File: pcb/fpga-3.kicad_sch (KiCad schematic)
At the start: 1 part

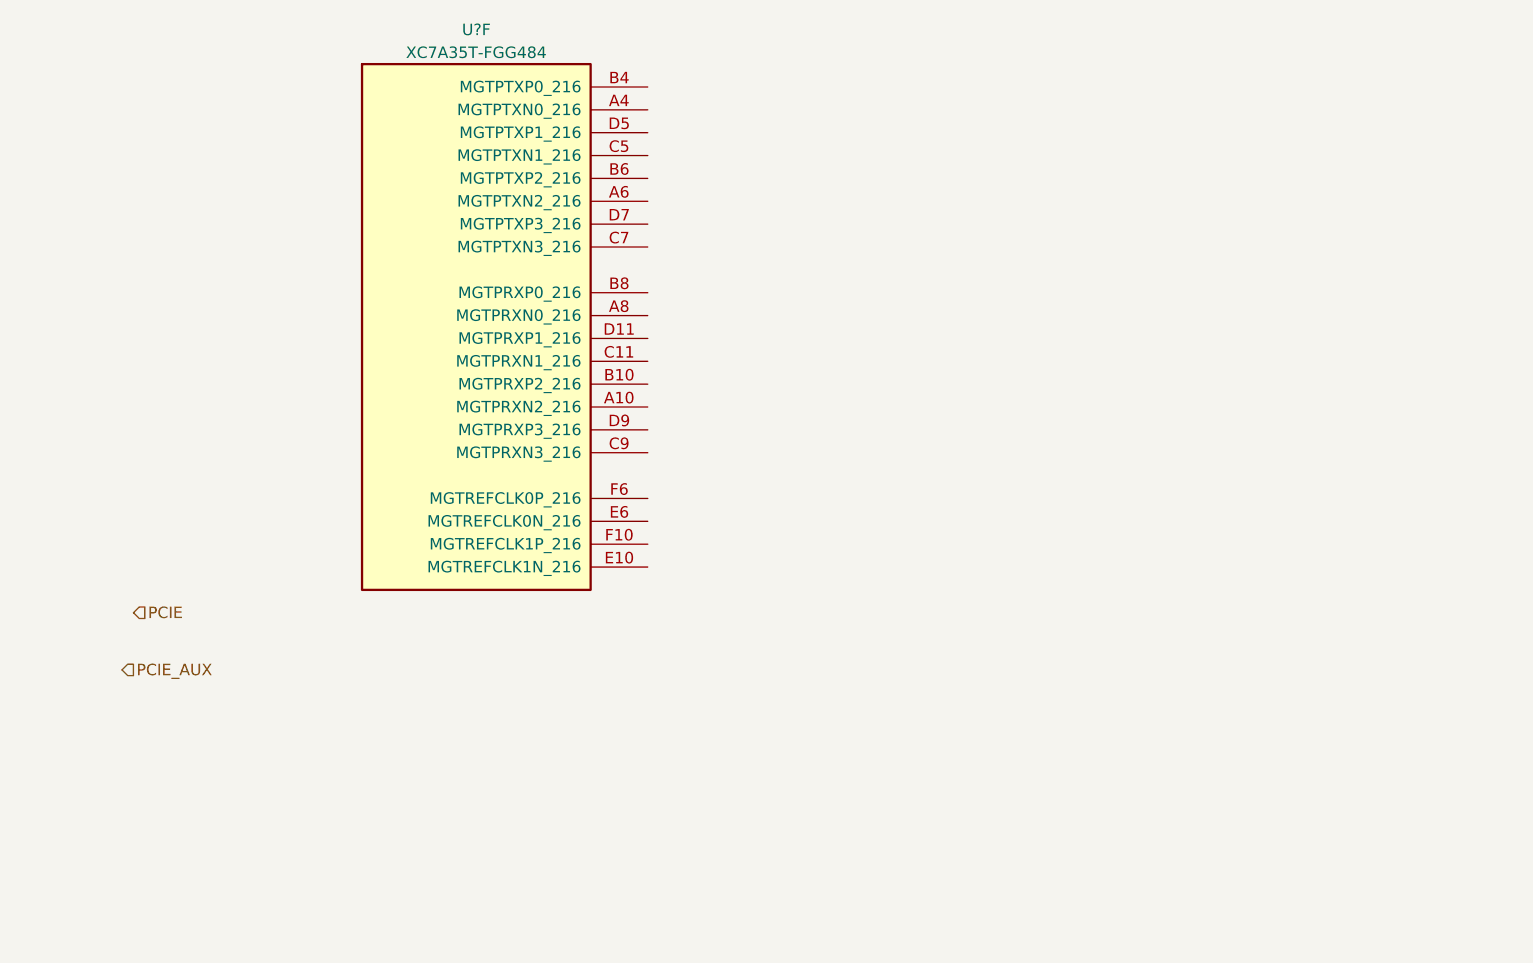
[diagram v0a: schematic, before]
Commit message: current sense, fpga power sequencing
plus restructuring files
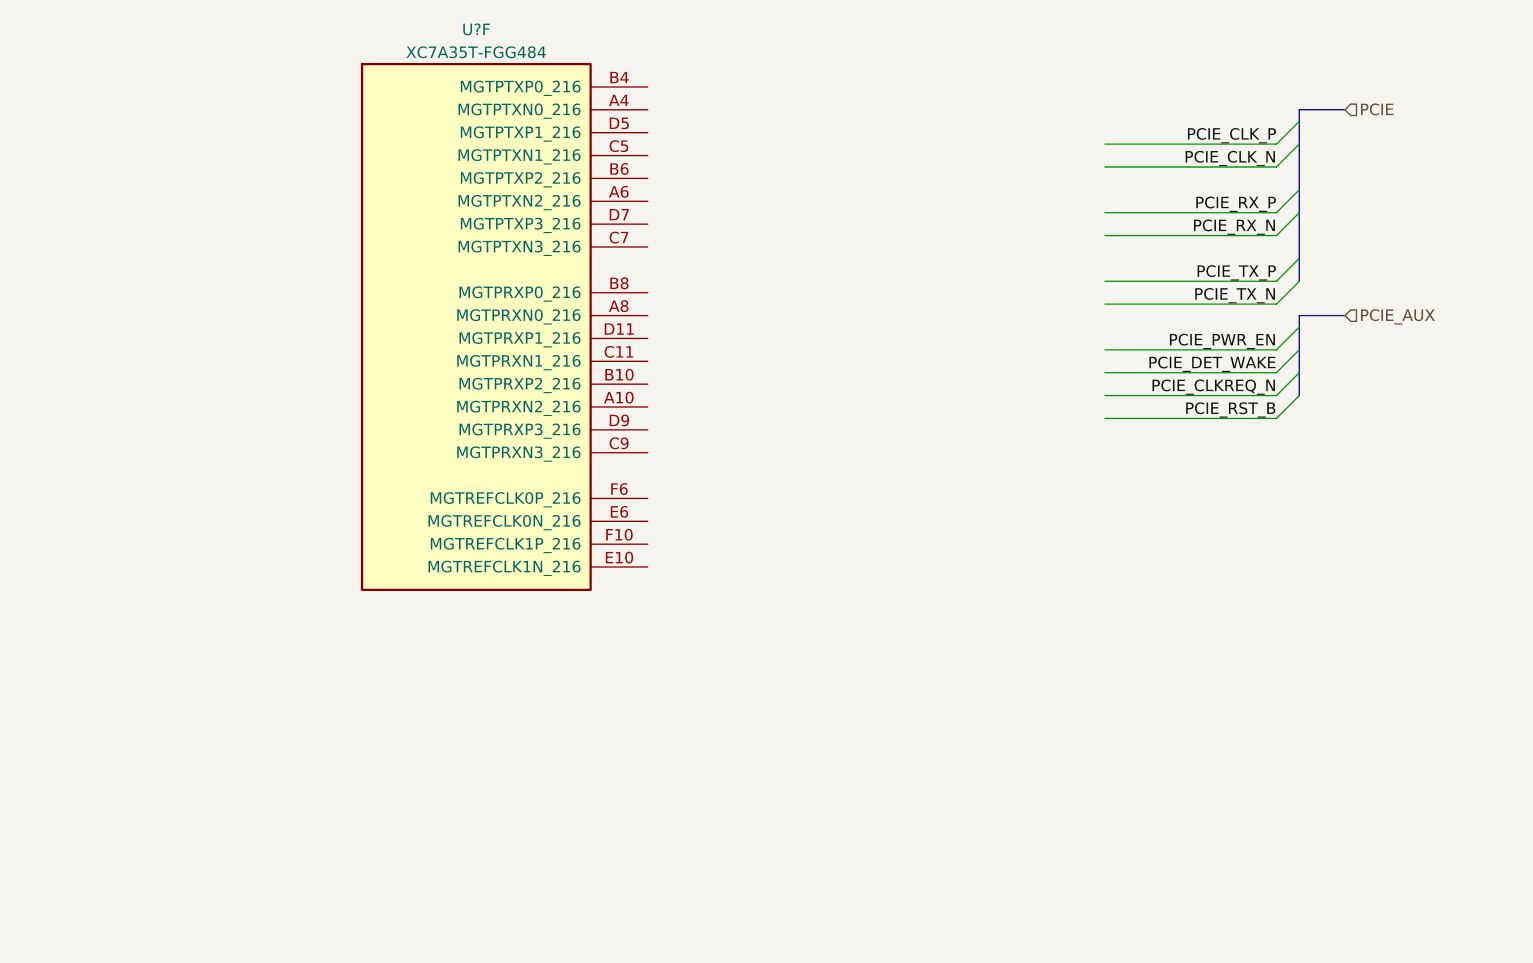
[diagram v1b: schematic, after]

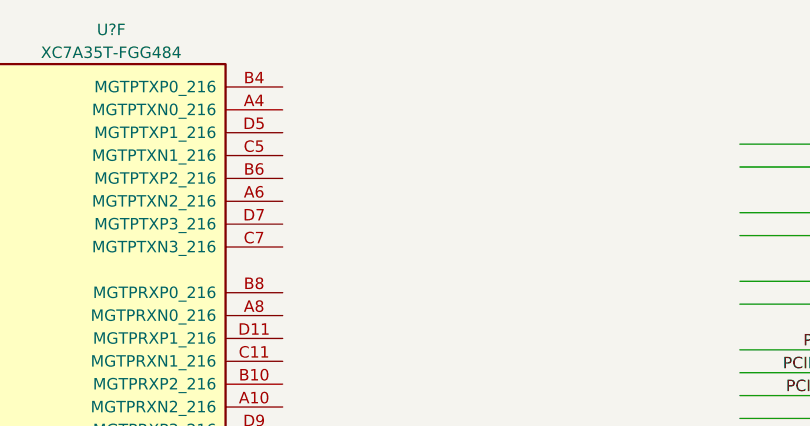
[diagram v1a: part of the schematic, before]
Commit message: add sensors, hierarchical changes
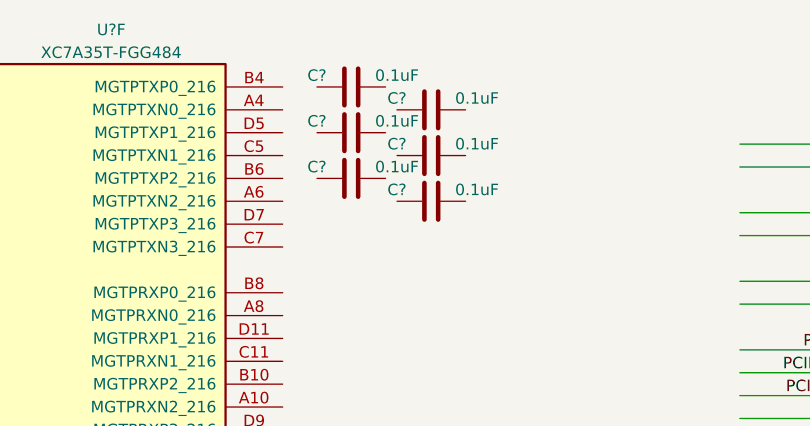
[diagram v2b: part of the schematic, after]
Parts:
- added C? (x6): 0.1uF, Capacitor_SMD:C_0402_1005Metric, symbol Device:C

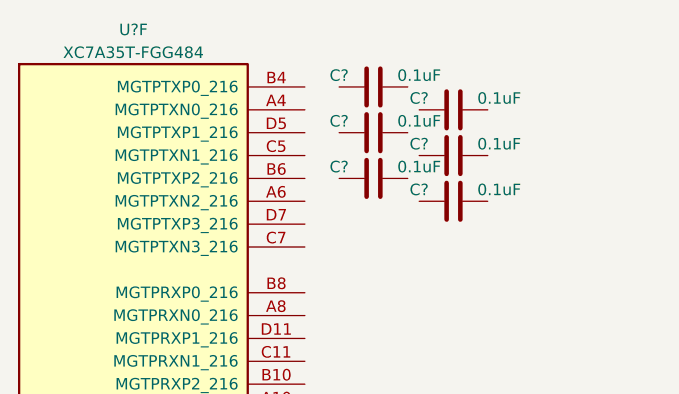
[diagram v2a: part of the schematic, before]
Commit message: addl. updates to power hierarchy
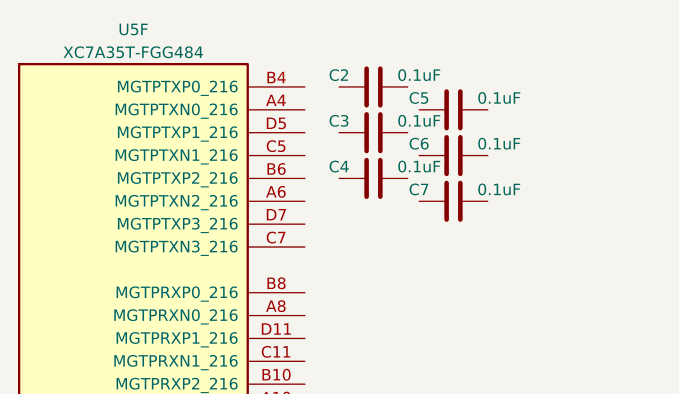
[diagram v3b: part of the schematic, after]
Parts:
- gave numbers to parts that had none: 7
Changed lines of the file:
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@@
 		(on_board yes)
 		(dnp no)
-		(property "Reference" "C?"
+		(property "Reference" "C5"
 			(at 175.26 54.61 90)
 			(effects
@@
 			(project "RPi-HwAB-1"
 				(path "/e63e39d7-6ac0-4ffd-8aa3-1841a4541b55/20a31476-4eec-4a3e-82d2-9314270dc40b"
-					(reference "C?")
+					(reference "C5")
 					(unit 1)
 				)
@@
 		(on_board yes)
 		(dnp no)
-		(property "Reference" "C?"
+		(property "Reference" "C6"
 			(at 175.26 59.69 90)
 			(effects
@@
 			(project "RPi-HwAB-1"
 				(path "/e63e39d7-6ac0-4ffd-8aa3-1841a4541b55/20a31476-4eec-4a3e-82d2-9314270dc40b"
-					(reference "C?")
+					(reference "C6")
 					(unit 1)
 				)
@@
 		(dnp no)
 		(fields_autoplaced yes)
-		(property "Reference" "U?"
+		(property "Reference" "U5"
 			(at 143.51 46.99 0)
 			(effects
@@
 			(project "RPi-HwAB-1"
 				(path "/e63e39d7-6ac0-4ffd-8aa3-1841a4541b55/20a31476-4eec-4a3e-82d2-9314270dc40b"
-					(reference "U?")
+					(reference "U5")
 					(unit 6)
 				)
@@
 		(on_board yes)
 		(dnp no)
-		(property "Reference" "C?"
+		(property "Reference" "C2"
 			(at 166.37 52.07 90)
 			(effects
@@
 			(project ""
 				(path "/e63e39d7-6ac0-4ffd-8aa3-1841a4541b55/20a31476-4eec-4a3e-82d2-9314270dc40b"
-					(reference "C?")
+					(reference "C2")
 					(unit 1)
 				)
@@
 		(on_board yes)
 		(dnp no)
-		(property "Reference" "C?"
+		(property "Reference" "C7"
 			(at 175.26 64.77 90)
 			(effects
@@
 			(project "RPi-HwAB-1"
 				(path "/e63e39d7-6ac0-4ffd-8aa3-1841a4541b55/20a31476-4eec-4a3e-82d2-9314270dc40b"
-					(reference "C?")
+					(reference "C7")
 					(unit 1)
 				)
@@
 		(on_board yes)
 		(dnp no)
-		(property "Reference" "C?"
+		(property "Reference" "C3"
 			(at 166.37 57.15 90)
 			(effects
@@
 			(project "RPi-HwAB-1"
 				(path "/e63e39d7-6ac0-4ffd-8aa3-1841a4541b55/20a31476-4eec-4a3e-82d2-9314270dc40b"
-					(reference "C?")
+					(reference "C3")
 					(unit 1)
 				)
@@
 		(on_board yes)
 		(dnp no)
-		(property "Reference" "C?"
+		(property "Reference" "C4"
 			(at 166.37 62.23 90)
 			(effects
@@
 			(project "RPi-HwAB-1"
 				(path "/e63e39d7-6ac0-4ffd-8aa3-1841a4541b55/20a31476-4eec-4a3e-82d2-9314270dc40b"
-					(reference "C?")
+					(reference "C4")
 					(unit 1)
 				)

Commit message: added power sequencing through raspi gpio
additionally defined sensors
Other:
- company: (none) -> Andre S Winkel
- title: (none) -> RPi HwAB HAT+
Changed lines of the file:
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@@
 	(generator_version "9.0")
 	(paper "A4")
+	(title_block
+		(title "RPi HwAB HAT+")
+		(date "2025-08-23")
+		(rev "01")
+		(company "Andre S Winkel")
+	)
 	(bus_entry
 		(at 232.41 59.69)

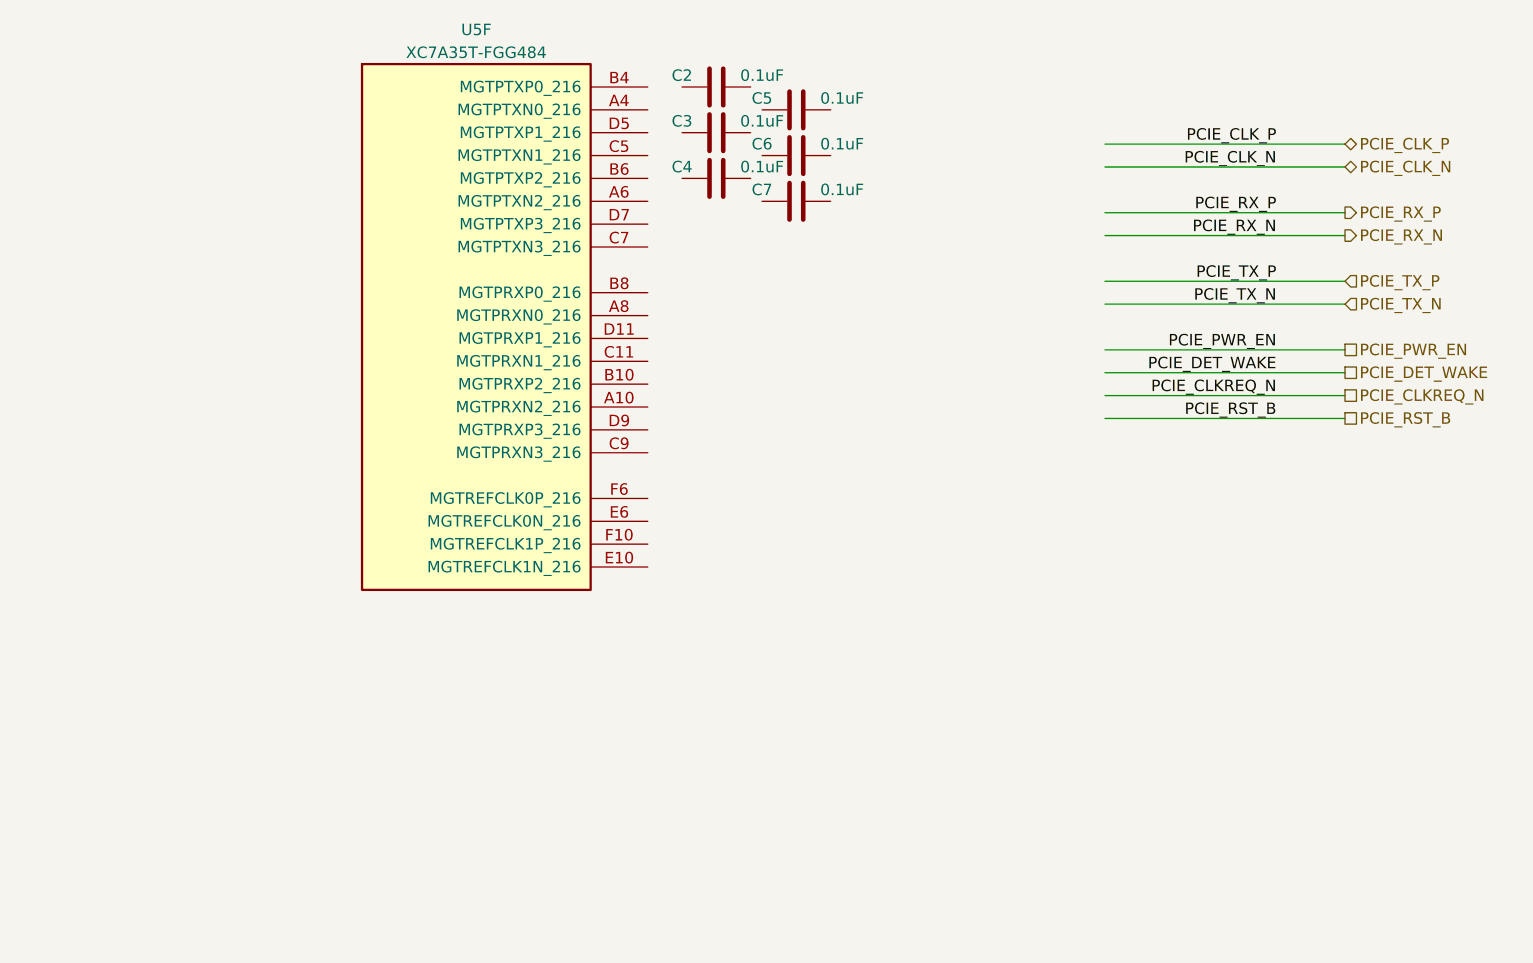
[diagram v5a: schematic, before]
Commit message: defined pcie diff. connections
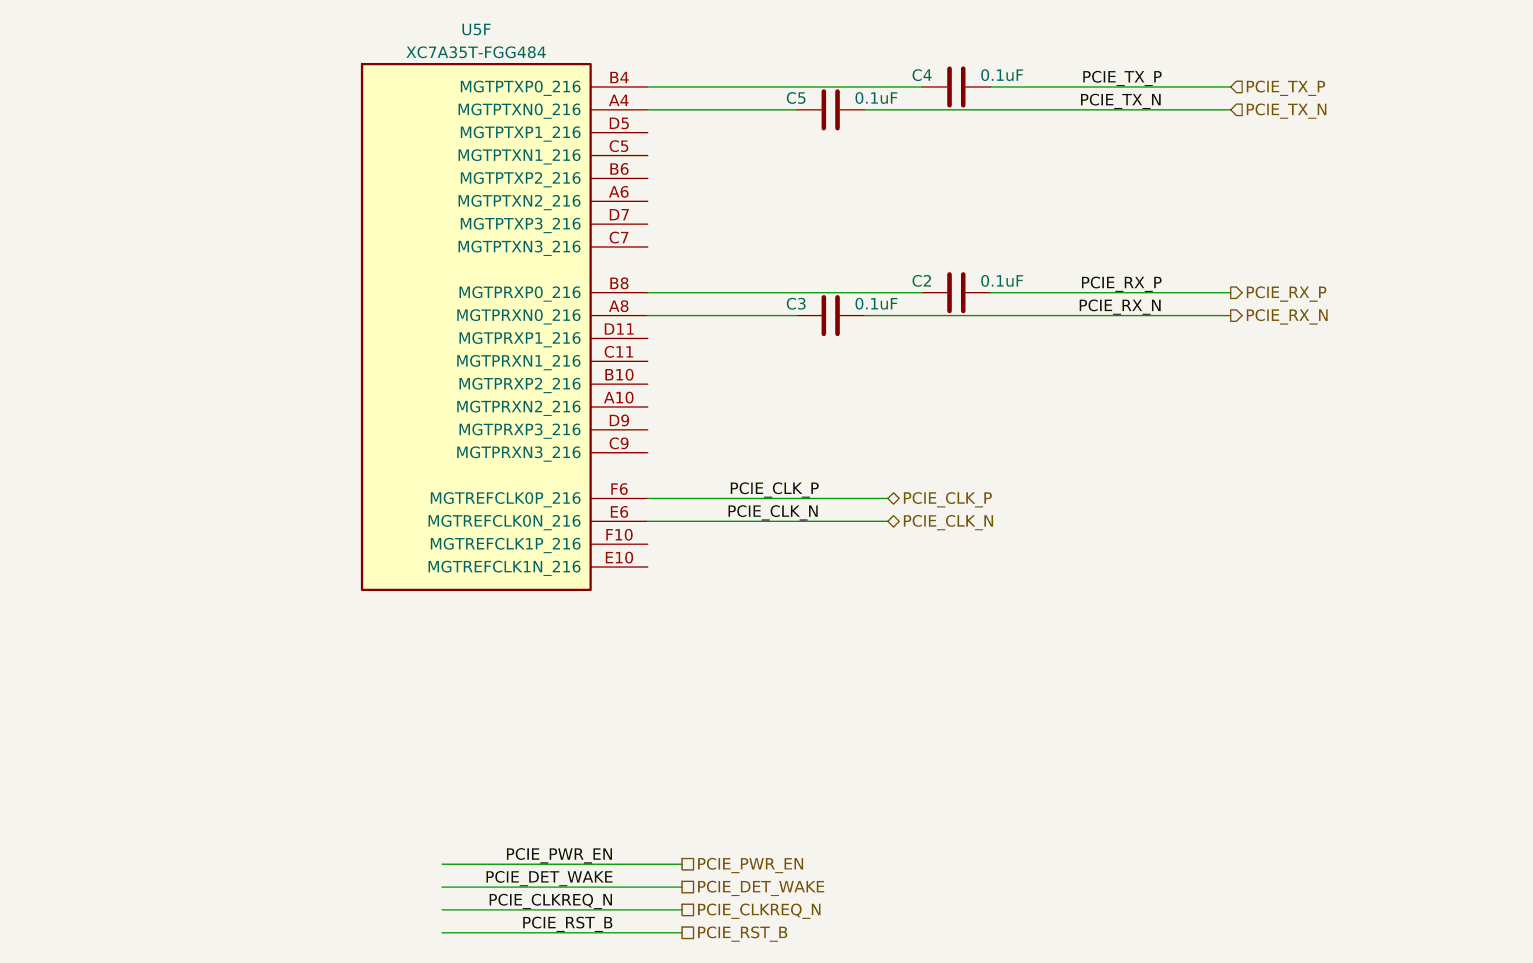
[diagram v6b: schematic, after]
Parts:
- removed C6, C7: 0.1uF, Capacitor_SMD:C_0402_1005Metric, symbol Device:C
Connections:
- net PCIE_CLK_N: now also U5.E6 (MGTREFCLK0N_216)
- net PCIE_CLK_P: now also U5.F6 (MGTREFCLK0P_216)
- net PCIE_RX_N: now also C3.2
- net PCIE_RX_P: now also C2.2
- net PCIE_TX_N: now also C5.2
- net PCIE_TX_P: now also C4.2
- net at C5.1: now also U5.A4 (MGTPTXN0_216)
- net at U5.A8 (MGTPRXN0_216): now also C3.1
- net at U5.B4 (MGTPTXP0_216): now also C4.1
- net at U5.B8 (MGTPRXP0_216): now also C2.1
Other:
- moved on the sheet: C2, C3, C4, C5
